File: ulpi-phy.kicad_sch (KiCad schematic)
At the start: 16 parts, among them U1701 USB3320C-EZK-TR, Y1701 Resonator_24MHz_ECX-1247

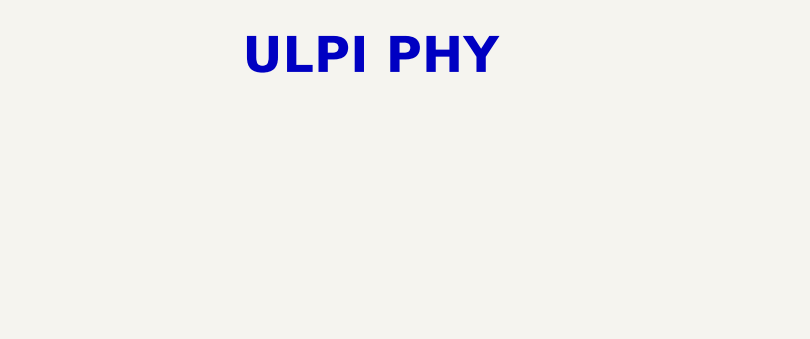
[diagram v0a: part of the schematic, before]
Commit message: [#100282] Add missing schematic sheet names and align them all
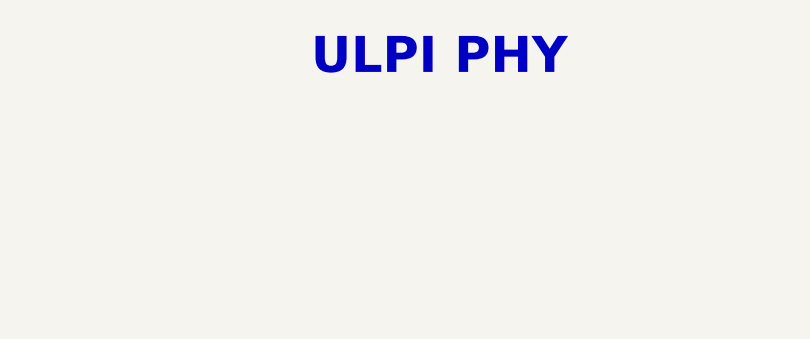
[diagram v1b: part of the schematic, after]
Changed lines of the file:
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@@
 	(text "ULPI PHY"
 		(exclude_from_sim no)
-		(at 203.2 38.1 0)
+		(at 210.82 38.1 0)
 		(effects
 			(font

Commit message: [#100501] Reannotate schematic
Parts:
- renumbered C1701 to C139, C1702 to C140, C1703 to C141, C1704 to C142, C1705 to C143, C1706 to C144, C1707 to C145, C1708 to C146, R1701 to R178, R1702 to R179, R1703 to R180, R1704 to R181, R1705 to R182, TP1701 to TP23, U1701 to U22, Y1701 to Y3

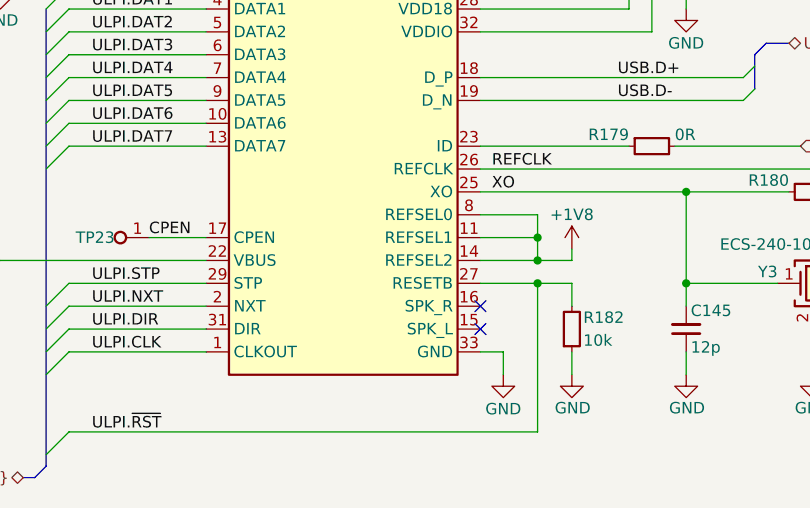
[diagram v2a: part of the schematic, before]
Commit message: [#100595] Update connections according to client request
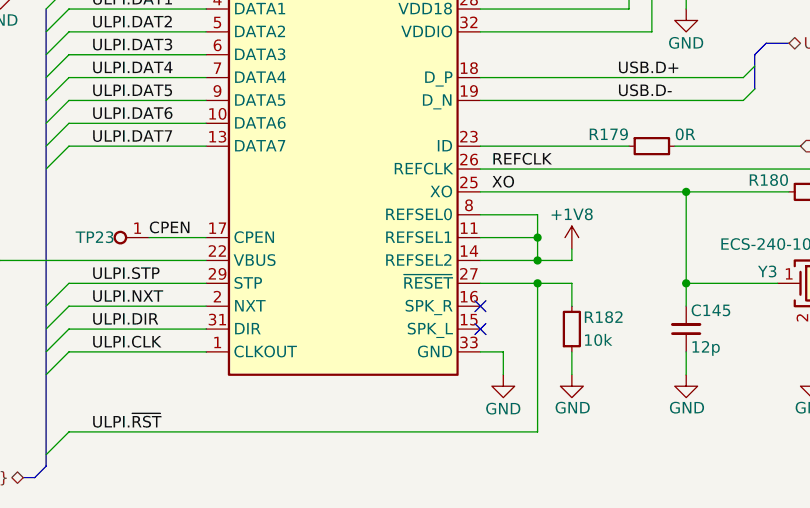
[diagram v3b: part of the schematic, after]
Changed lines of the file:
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@@
 			(justify right bottom)
 		)
-		(property "Net Class" "90Ohm-diff"
+		(property "Netclass" "90Ohm-diff"
 			(at 256.54 138.43 0)
 			(show_name no)
@@
 			(justify left bottom)
 		)
-		(property "Net Class" "50Ohm-se"
+		(property "Netclass" "50Ohm-se"
 			(at 170.18 179.07 0)
 			(show_name no)

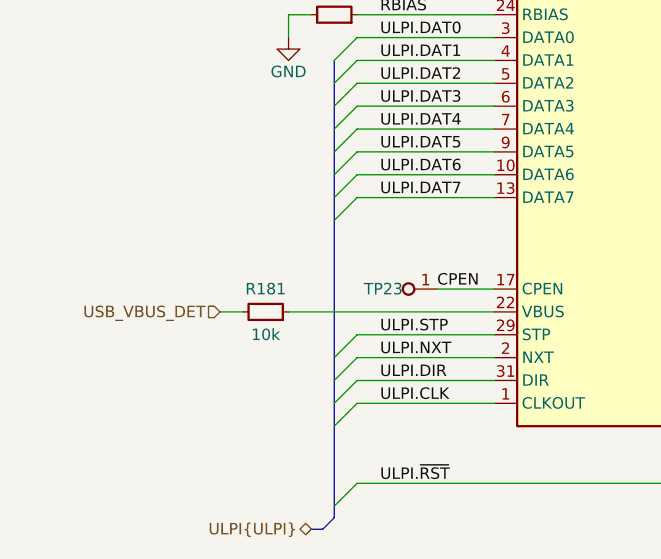
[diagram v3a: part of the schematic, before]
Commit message: [#100501] Connect ULPI CPEN signal to USB hub VBUS_DET
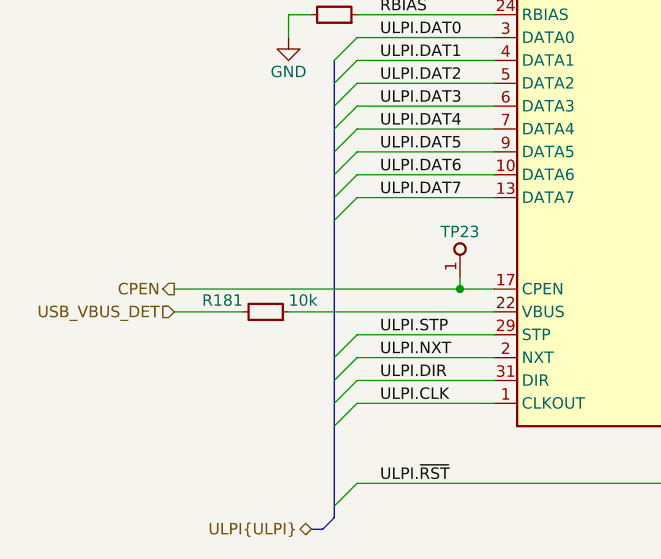
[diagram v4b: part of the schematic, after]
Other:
- moved on the sheet: TP23
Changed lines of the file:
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@@
 	)
 	(junction
+		(at 187.96 157.48)
+		(diameter 0)
+		(color 0 0 0 0)
+	)
+	(junction
 		(at 262.89 105.41)
 		(diameter 0)
@@
 	(wire
 		(pts
-			(xy 185.42 157.48) (xy 191.77 157.48)
-		)
-		(stroke
-			(width 0)
-			(type default)
-		)
-	)
-	(wire
-		(pts
 			(xy 168.91 127) (xy 171.45 127)
 		)
@@
 	(wire
 		(pts
+			(xy 187.96 156.21) (xy 187.96 157.48)
+		)
+		(stroke
+			(width 0)
+			(type default)
+		)
+	)
+	(wire
+		(pts
 			(xy 238.76 147.32) (xy 222.25 147.32)
 		)
@@
 	(wire
 		(pts
+			(xy 187.96 157.48) (xy 191.77 157.48)
+		)
+		(stroke
+			(width 0)
+			(type default)
+		)
+	)
+	(wire
+		(pts
 			(xy 222.25 157.48) (xy 228.6 157.48)
 		)
@@
 		)
 	)
+	(wire
+		(pts
+			(xy 156.21 157.48) (xy 187.96 157.48)
+		)
+		(stroke
+			(width 0)
+			(type default)
+		)
+	)
 	(bus
 		(pts
@@
 	(wire
 		(pts
-			(xy 161.29 160.02) (xy 163.83 160.02)
+			(xy 156.21 160.02) (xy 163.83 160.02)
 		)
 		(stroke
@@
 		)
 	)
-	(label "CPEN"
-		(at 185.42 157.48 0)
-		(effects
-			(font
-				(size 1.27 1.27)
-			)
-			(justify left bottom)
-		)
-	)
 	(label "RBIAS"
 		(at 179.07 127 0)
@@
 	(hierarchical_label "USB_VBUS_DET"
 		(shape input)
-		(at 161.29 160.02 180)
+		(at 156.21 160.02 180)
+		(effects
+			(font
+				(size 1.27 1.27)
+			)
+			(justify right)
+		)
+	)
+	(hierarchical_label "CPEN"
+		(shape output)
+		(at 156.21 157.48 180)
 		(effects
 			(font
@@
 		(dnp no)
 		(property "Reference" "R181"
-			(at 166.37 157.48 0)
+			(at 163.83 158.75 0)
 			(show_name no)
 			(do_not_autoplace no)
@@
 					(thickness 0.15)
 				)
+				(justify left)
 			)
 		)
@@
 		)
 		(property "Val" "10k"
-			(at 166.37 162.56 0)
+			(at 168.91 158.75 0)
 			(show_name no)
 			(do_not_autoplace no)
@@
 					(thickness 0.15)
 				)
+				(justify right)
 			)
 		)
@@
 	(symbol
 		(lib_id "antmicroTestPoints:TP_0.75mm_SMD")
-		(at 185.42 157.48 180)
+		(at 187.96 156.21 90)
 		(unit 1)
 		(body_style 1)
@@
 		(dnp no)
 		(property "Reference" "TP23"
-			(at 181.61 157.48 0)
+			(at 187.96 151.13 90)
 			(show_name no)
 			(do_not_autoplace no)
@@
 					(thickness 0.15)
 				)
-				(justify left)
 			)
 		)
 		(property "Value" "TP_0.75mm_SMD"
-			(at 175.26 153.67 0)
+			(at 191.77 146.05 0)
 			(hide yes)
 			(show_name no)
@@
 		)
 		(property "Footprint" "antmicro-footprints:TP_SMD_0.75mm"
-			(at 175.26 151.13 0)
+			(at 194.31 146.05 0)
 			(hide yes)
 			(show_name no)
@@
 		)
 		(property "Datasheet" ""
-			(at 167.64 144.78 0)
+			(at 200.66 138.43 0)
 			(hide yes)
 			(show_name no)
@@
 		)
 		(property "Description" "SMT test point"
-			(at 174.625 143.51 0)
+			(at 201.93 145.415 0)
 			(hide yes)
 			(show_name no)
@@
 		)
 		(property "MPN" ""
-			(at 174.625 146.05 0)
+			(at 199.39 145.415 0)
 			(hide yes)
 			(show_name no)
@@
 		)
 		(property "Manufacturer" ""
-			(at 174.625 151.13 0)
+			(at 194.31 145.415 0)
 			(hide yes)
 			(show_name no)
@@
 		)
 		(property "Author" "Antmicro"
-			(at 175.26 148.59 0)
+			(at 196.85 146.05 0)
 			(hide yes)
 			(show_name no)
@@
 		)
 		(property "License" "Apache-2.0"
-			(at 175.26 146.05 0)
+			(at 199.39 146.05 0)
 			(hide yes)
 			(show_name no)

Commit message: [#100501] Reannotate schematic
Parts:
- renumbered C139 to C144, C140 to C145, C141 to C146, C142 to C147, C143 to C148, C144 to C149, C145 to C150, C146 to C151, R178 to R223, R179 to R224, R180 to R225, R181 to R226, R182 to R227, TP23 to TP27, U22 to U21

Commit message: [#100501] Perform minor BOM consolidation
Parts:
- C145, C146, C147, C149: value C_1u_0402 -> C_1u_25V_0402; symbol antmicroCapacitors0402:C_1u_0402 -> antmicroCapacitors0402:C_1u_25V_0402; Dielectric (none) -> X5R; MPN C1005X6S1A105K050BC -> GRM155R61E105KE11J; Manufacturer TDK -> Murata; Voltage (none) -> 25V
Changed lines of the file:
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@@
 	)
 	(symbol
-		(lib_id "antmicroCapacitors0402:C_1u_0402")
+		(lib_id "antmicroCapacitors0402:C_1u_25V_0402")
 		(at 232.41 113.03 270)
 		(mirror x)
@@
 			)
 		)
-		(property "Value" "C_1u_0402"
+		(property "Value" "C_1u_25V_0402"
 			(at 222.25 92.71 0)
 			(hide yes)
@@
 			)
 		)
-		(property "Datasheet" "https://product.tdk.com/en/search/capacitor/ceramic/mlcc/info?part_no=C1005X6S1A105K050BC"
+		(property "Datasheet" "https://www.murata.com/products/productdetail?partno=GRM155R61E105KE11%23"
 			(at 217.17 92.71 0)
 			(hide yes)
@@
 			)
 		)
-		(property "Description" "SMD Multilayer Ceramic Capacitor, 1 µF, 10 V, 0402 [1005 Metric], ± 10%, X6S, C"
+		(property "Description" "SMD Multilayer Ceramic Capacitor, 1 µF, 25 V, 0402 [1005 Metric], ± 10%, X5R, GRM Series"
 			(at 199.39 92.71 0)
 			(hide yes)
@@
 			)
 		)
-		(property "MPN" "C1005X6S1A105K050BC"
+		(property "MPN" "GRM155R61E105KE11J"
 			(at 214.63 92.71 0)
 			(hide yes)
@@
 			)
 		)
-		(property "Manufacturer" "TDK"
+		(property "Manufacturer" "Murata"
 			(at 212.09 92.71 0)
 			(hide yes)
@@
 			)
 		)
-		(property "Voltage" ""
+		(property "Voltage" "25V"
 			(at 204.47 92.71 0)
 			(hide yes)
@@
 			)
 		)
-		(property "Dielectric" ""
+		(property "Dielectric" "X5R"
 			(at 201.93 92.71 0)
 			(hide yes)
@@
 	)
 	(symbol
-		(lib_id "antmicroCapacitors0402:C_1u_0402")
+		(lib_id "antmicroCapacitors0402:C_1u_25V_0402")
 		(at 245.11 113.03 90)
 		(unit 1)
@@
 			)
 		)
-		(property "Value" "C_1u_0402"
+		(property "Value" "C_1u_25V_0402"
 			(at 255.27 92.71 0)
 			(hide yes)
@@
 			)
 		)
-		(property "Datasheet" "https://product.tdk.com/en/search/capacitor/ceramic/mlcc/info?part_no=C1005X6S1A105K050BC"
+		(property "Datasheet" "https://www.murata.com/products/productdetail?partno=GRM155R61E105KE11%23"
 			(at 260.35 92.71 0)
 			(hide yes)
@@
 			)
 		)
-		(property "Description" "SMD Multilayer Ceramic Capacitor, 1 µF, 10 V, 0402 [1005 Metric], ± 10%, X6S, C"
+		(property "Description" "SMD Multilayer Ceramic Capacitor, 1 µF, 25 V, 0402 [1005 Metric], ± 10%, X5R, GRM Series"
 			(at 278.13 92.71 0)
 			(hide yes)
@@
 			)
 		)
-		(property "MPN" "C1005X6S1A105K050BC"
+		(property "MPN" "GRM155R61E105KE11J"
 			(at 262.89 92.71 0)
 			(hide yes)
@@
 			)
 		)
-		(property "Manufacturer" "TDK"
+		(property "Manufacturer" "Murata"
 			(at 265.43 92.71 0)
 			(hide yes)
@@
 			)
 		)
-		(property "Voltage" ""
+		(property "Voltage" "25V"
 			(at 273.05 92.71 0)
 			(hide yes)
@@
 			)
 		)
-		(property "Dielectric" ""
+		(property "Dielectric" "X5R"
 			(at 275.59 92.71 0)
 			(hide yes)
@@
 	)
 	(symbol
-		(lib_id "antmicroCapacitors0402:C_1u_0402")
+		(lib_id "antmicroCapacitors0402:C_1u_25V_0402")
 		(at 245.11 129.54 90)
 		(unit 1)
@@
 			)
 		)
-		(property "Value" "C_1u_0402"
+		(property "Value" "C_1u_25V_0402"
 			(at 255.27 109.22 0)
 			(hide yes)
@@
 			)
 		)
-		(property "Datasheet" "https://product.tdk.com/en/search/capacitor/ceramic/mlcc/info?part_no=C1005X6S1A105K050BC"
+		(property "Datasheet" "https://www.murata.com/products/productdetail?partno=GRM155R61E105KE11%23"
 			(at 260.35 109.22 0)
 			(hide yes)
@@
 			)
 		)
-		(property "Description" "SMD Multilayer Ceramic Capacitor, 1 µF, 10 V, 0402 [1005 Metric], ± 10%, X6S, C"
+		(property "Description" "SMD Multilayer Ceramic Capacitor, 1 µF, 25 V, 0402 [1005 Metric], ± 10%, X5R, GRM Series"
 			(at 278.13 109.22 0)
 			(hide yes)
@@
 			)
 		)
-		(property "MPN" "C1005X6S1A105K050BC"
+		(property "MPN" "GRM155R61E105KE11J"
 			(at 262.89 109.22 0)
 			(hide yes)
@@
 			)
 		)
-		(property "Manufacturer" "TDK"
+		(property "Manufacturer" "Murata"
 			(at 265.43 109.22 0)
 			(hide yes)
@@
 			)
 		)
-		(property "Voltage" ""
+		(property "Voltage" "25V"
 			(at 273.05 109.22 0)
 			(hide yes)
@@
 			)
 		)
-		(property "Dielectric" ""
+		(property "Dielectric" "X5R"
 			(at 275.59 109.22 0)
 			(hide yes)
@@
 	)
 	(symbol
-		(lib_id "antmicroCapacitors0402:C_1u_0402")
+		(lib_id "antmicroCapacitors0402:C_1u_25V_0402")
 		(at 254 113.03 90)
 		(unit 1)
@@
 			)
 		)
-		(property "Value" "C_1u_0402"
+		(property "Value" "C_1u_25V_0402"
 			(at 264.16 92.71 0)
 			(hide yes)
@@
 			)
 		)
-		(property "Datasheet" "https://product.tdk.com/en/search/capacitor/ceramic/mlcc/info?part_no=C1005X6S1A105K050BC"
+		(property "Datasheet" "https://www.murata.com/products/productdetail?partno=GRM155R61E105KE11%23"
 			(at 269.24 92.71 0)
 			(hide yes)
@@
 			)
 		)
-		(property "Description" "SMD Multilayer Ceramic Capacitor, 1 µF, 10 V, 0402 [1005 Metric], ± 10%, X6S, C"
+		(property "Description" "SMD Multilayer Ceramic Capacitor, 1 µF, 25 V, 0402 [1005 Metric], ± 10%, X5R, GRM Series"
 			(at 287.02 92.71 0)
 			(hide yes)
@@
 			)
 		)
-		(property "MPN" "C1005X6S1A105K050BC"
+		(property "MPN" "GRM155R61E105KE11J"
 			(at 271.78 92.71 0)
 			(hide yes)
@@
 			)
 		)
-		(property "Manufacturer" "TDK"
+		(property "Manufacturer" "Murata"
 			(at 274.32 92.71 0)
 			(hide yes)
@@
 			)
 		)
-		(property "Voltage" ""
+		(property "Voltage" "25V"
 			(at 281.94 92.71 0)
 			(hide yes)
@@
 			)
 		)
-		(property "Dielectric" ""
+		(property "Dielectric" "X5R"
 			(at 284.48 92.71 0)
 			(hide yes)
